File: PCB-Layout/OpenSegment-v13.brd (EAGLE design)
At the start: 35.6 x 38.1 mm, 51 parts, among them Q1 PNP, Q10 MMBT2222, Q11 MMBT2222, Q12 MMBT2222, Q2 PNP, Q3 PNP, Q4 PNP, Q5 PNP, Q6 PNP, Q7 PNP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

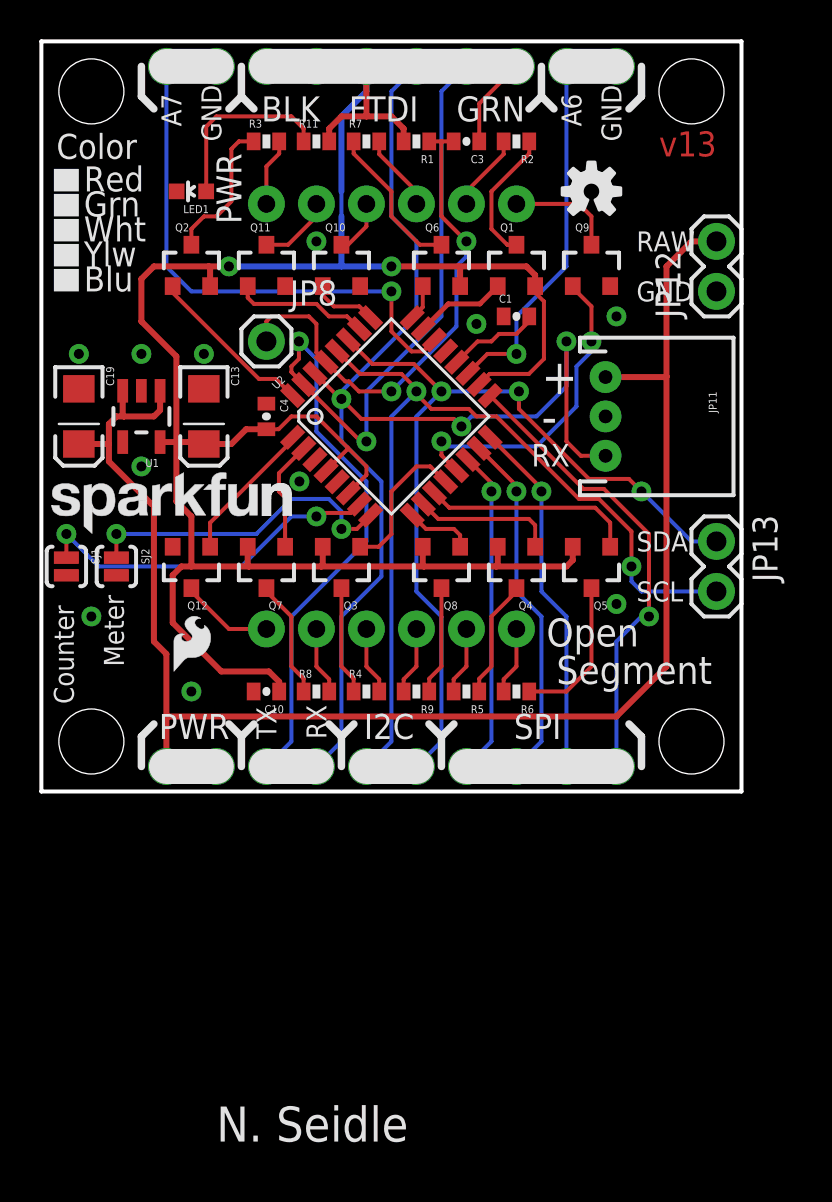
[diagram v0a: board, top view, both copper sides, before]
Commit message: Added fiducial markings and created panel
preparing for mass production
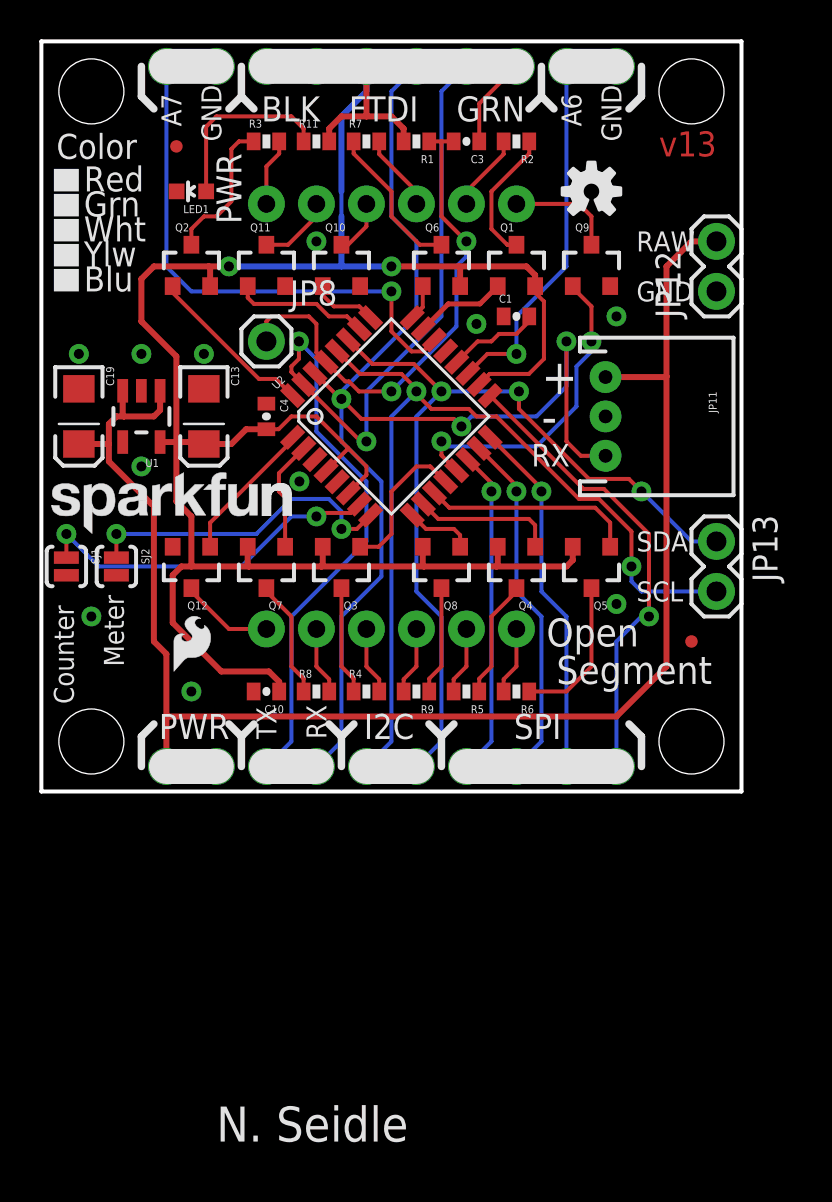
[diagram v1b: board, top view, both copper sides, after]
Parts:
- added JP14, JP7: FIDUCIALUFIDUCIAL, SparkFun:MICRO-FIDUCIAL

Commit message: Updated resistor values.
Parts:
- R2, R3, R4, R5, R6, R7, R8, R9: value 27 -> 33/68
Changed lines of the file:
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@@
 <element name="JP5" library="SparkFun-Electromechanical" package="STAND-OFF" value="STAND-OFF" x="15.24" y="-16.51"/>
 <element name="JP6" library="SparkFun-Electromechanical" package="STAND-OFF" value="STAND-OFF" x="-15.24" y="-16.51"/>
-<element name="R2" library="SparkFun" package="0402-RES" value="27" x="6.35" y="13.97" rot="R180"/>
+<element name="R2" library="SparkFun" package="0402-RES" value="33/68" x="6.35" y="13.97" rot="R180"/>
 <element name="Q1" library="SparkFun-DiscreteSemi" package="SOT23-3" value="PNP" x="6.35" y="7.62"/>
 <element name="SJ2" library="SparkFun-Passives" package="SJ_2S-NO" value="Counter Ctl" x="-13.97" y="-7.62" smashed="yes" rot="R270">
@@
 </element>
 <element name="JP2" library="SparkFun-Connectors" package="1X10" value="Connections" x="11.43" y="-17.78" rot="MR0"/>
-<element name="R3" library="SparkFun" package="0402-RES" value="27" x="-6.35" y="13.97"/>
-<element name="R4" library="SparkFun" package="0402-RES" value="27" x="-1.27" y="-13.97"/>
-<element name="R5" library="SparkFun" package="0402-RES" value="27" x="3.81" y="-13.97" rot="R180"/>
-<element name="R6" library="SparkFun" package="0402-RES" value="27" x="6.35" y="-13.97" rot="R180"/>
-<element name="R7" library="SparkFun" package="0402-RES" value="27" x="-1.27" y="13.97"/>
-<element name="R8" library="SparkFun" package="0402-RES" value="27" x="-3.81" y="-13.97"/>
-<element name="R9" library="SparkFun" package="0402-RES" value="27" x="1.27" y="-13.97" rot="R180"/>
+<element name="R3" library="SparkFun" package="0402-RES" value="33/68" x="-6.35" y="13.97"/>
+<element name="R4" library="SparkFun" package="0402-RES" value="33/68" x="-1.27" y="-13.97"/>
+<element name="R5" library="SparkFun" package="0402-RES" value="33/68" x="3.81" y="-13.97" rot="R180"/>
+<element name="R6" library="SparkFun" package="0402-RES" value="33/68" x="6.35" y="-13.97" rot="R180"/>
+<element name="R7" library="SparkFun" package="0402-RES" value="33/68" x="-1.27" y="13.97"/>
+<element name="R8" library="SparkFun" package="0402-RES" value="33/68" x="-3.81" y="-13.97"/>
+<element name="R9" library="SparkFun" package="0402-RES" value="33/68" x="1.27" y="-13.97" rot="R180"/>
 <element name="U$1" library="SparkFun" package="SFE-LOGO-FLAME" value="LOGO-SFESK" x="-12.192" y="-16.129" rot="MR0"/>
 <element name="Q9" library="SparkFun-DiscreteSemi" package="SOT23-3" value="MMBT2222" x="10.16" y="7.62"/>
